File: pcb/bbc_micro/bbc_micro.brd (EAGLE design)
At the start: 56 x 65 mm, 51 parts, among them IC1 STM32F072C8T6, SW1 324_SW, SW2 324_SW, SW3 324_SW

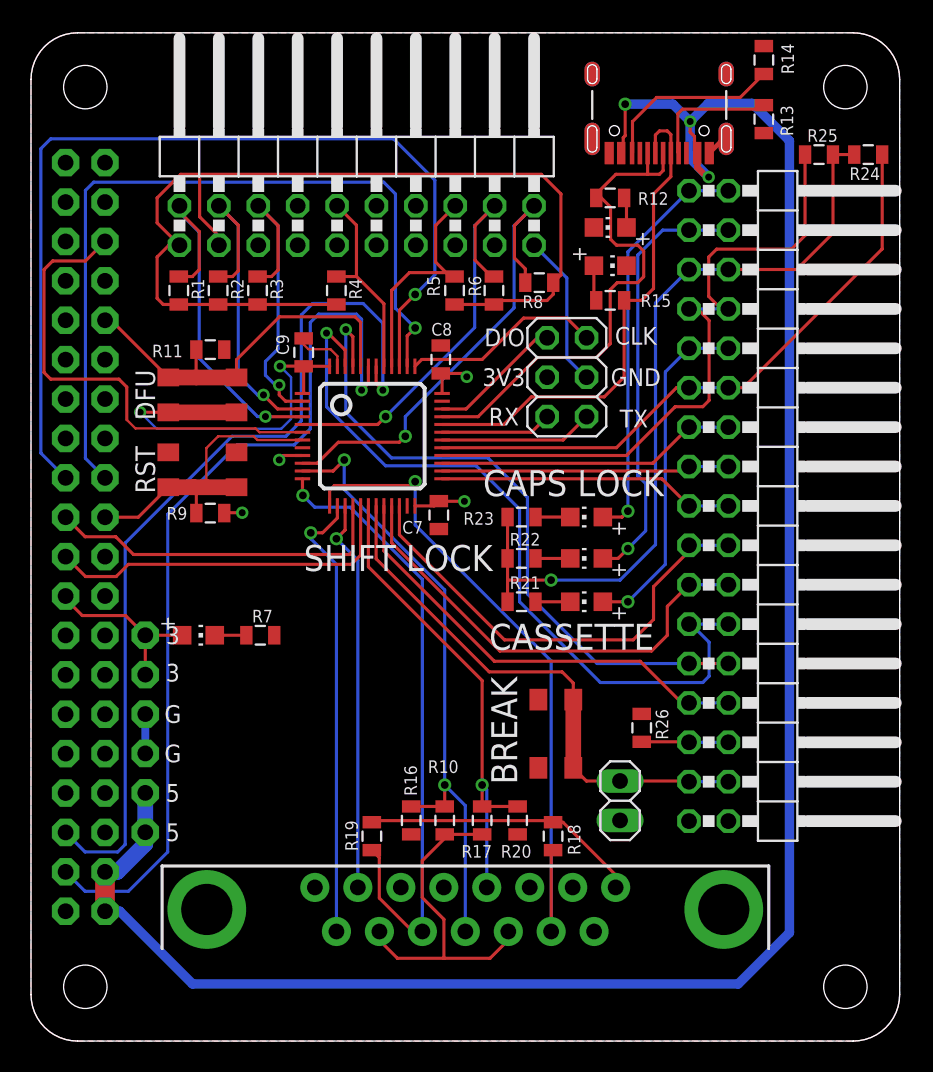
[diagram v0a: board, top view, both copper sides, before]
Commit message: removed second joystick and added BBC VREF input
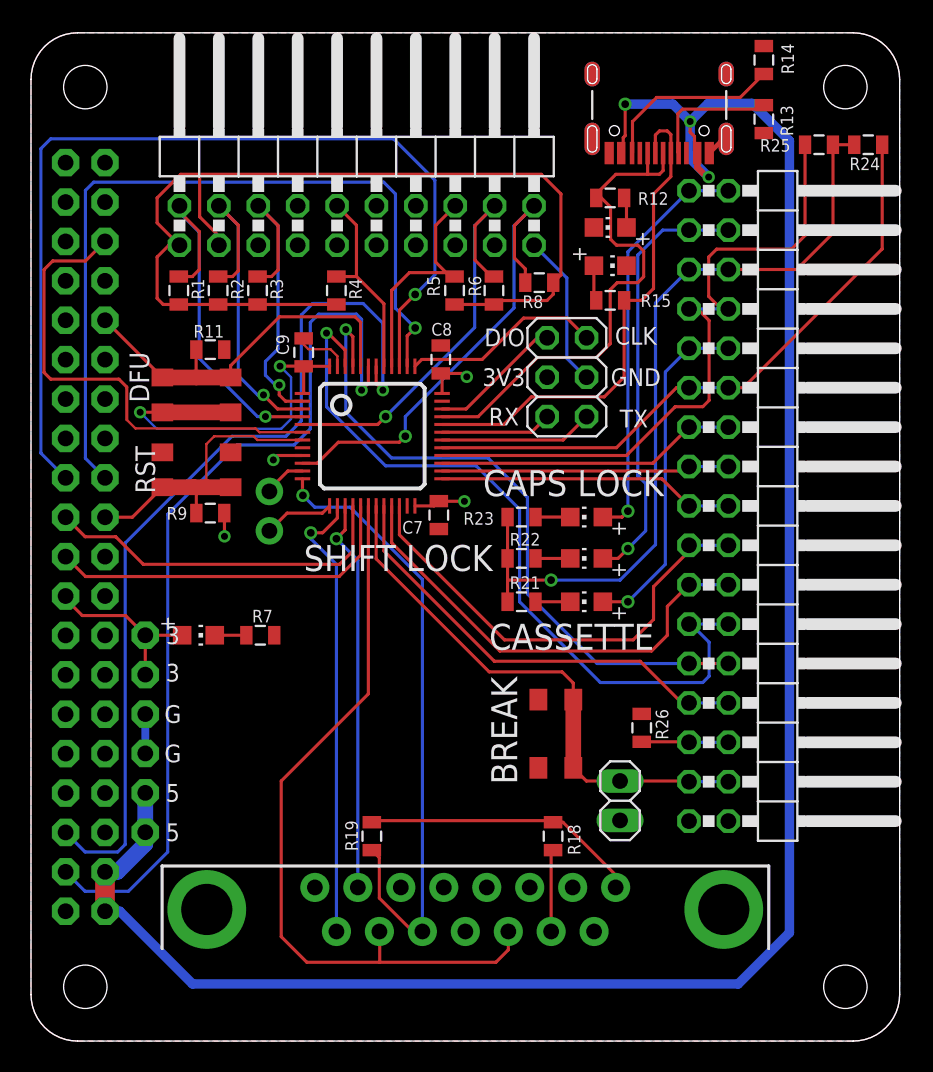
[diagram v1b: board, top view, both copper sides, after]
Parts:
- removed R10, R16, R17, R20: 5.1K, SparkFun-Passives:0805
- added JP10, JP11: (no value), adafruit_changed:1X01-CLEANBIG
- moved R24 0.63 mm to (54.0, 57.8)
- moved R25 0.63 mm to (50.8, 57.8)
- moved SW1 0.38 mm to (10.7, 36.8)
- moved SW2 0.38 mm to (10.7, 41.7)
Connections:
- removed net N$17: IC1.11, R10.2, R16.1, U$9.12
- new net N$11: IC1.11, JP10.1
- net GND: no longer R16.2, R20.2
- net N$10: now also IC1.18; no longer R10.1, R17.1
- net N$12: now also IC1.13, JP11.1; no longer IC1.18, R17.2, R20.1, U$9.4
- net N$21: no longer IC1.13
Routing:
- net N$17: track 40.2 -> 0.00 mm, vias 2 -> 0
- net N$21: track 44.7 -> 5.30 mm, vias 1 -> 0
- net N$10: track 22.0 -> 48.9 mm
- net N$12: track 31.4 -> 4.55 mm, vias 1 -> 0
- net N$11: track 0.00 -> 2.75 mm
- net CA2: track 44.1 -> 44.8 mm
- net W: track 39.8 -> 40.4 mm
- net KB_5V: track 51.3 -> 51.9 mm
- net SPI_MISO: track 22.5 -> 23.0 mm

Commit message: added a pot, clean up
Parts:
- added R10: (no value), SparkFun-Retired:TRIM_POT_PTH
- moved R24 0.13 mm to (54.0, 57.9)
- moved R25 0.13 mm to (50.8, 57.9)
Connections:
- net +3V3: now also R10.3
- net GND: now also R10.1
- net N$12: now also R10.2
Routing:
- net N$12: track 4.55 -> 14.2 mm
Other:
- board text added: "ACT"
- board text added: "ERR"
- board text added: "PIN1"
- board text added: "PT4 dekuNukem OCT2022"
- board text added: "PWR"
- board text removed: "PT3 dekuNukem SEPT2022"
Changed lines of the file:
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@@
 <text x="38.989" y="42.799" size="1.143" layer="25" rot="R180" align="center">GND</text>
 <text x="34.9758" y="35.9664" size="1.6764" layer="25" align="center">CAPS LOCK</text>
-<text x="7.366" y="36.83" size="1.27" layer="25" rot="R90" align="center">RST</text>
+<text x="6.858" y="36.83" size="1.27" layer="25" rot="R90" align="center">RST</text>
 <text x="30.48" y="40.259" size="1.143" layer="25" rot="R180" align="center">RX</text>
 <text x="38.862" y="40.132" size="1.143" layer="25" rot="R180" align="center">TX</text>
-<text x="6.985" y="42.799" size="1.27" layer="25" rot="R90" align="center">DFU</text>
+<text x="6.858" y="42.799" size="1.27" layer="25" rot="R90" align="center">DFU</text>
 <text x="24.3078" y="24.2316" size="1.778" layer="26" rot="MR180" align="center">USB4VC Protocol Card for
 BBC Micro
 </text>
-<text x="24.4348" y="21.1836" size="1.6764" layer="26" rot="MR180" align="center">PT3 dekuNukem SEPT2022</text>
+<text x="24.4348" y="21.1836" size="1.6764" layer="26" rot="MR180" align="center">PT4 dekuNukem OCT2022</text>
 <text x="24.8158" y="17.5006" size="1.9304" layer="26" rot="MR180" align="center">usb4vc.com</text>
 <text x="9.144" y="13.462" size="1.143" layer="25" rot="R180" align="center">5</text>
@@
 <text x="23.6728" y="31.1404" size="1.6764" layer="25" align="center">SHIFT LOCK</text>
 <text x="30.5054" y="20.0152" size="1.6764" layer="25" rot="R270" align="center">BREAK</text>
+<text x="40.386" y="53.34" size="1.4224" layer="25" rot="R270" align="center">ERR</text>
+<text x="40.386" y="48.768" size="1.4224" layer="25" rot="R270" align="center">ACT</text>
+<text x="10.795" y="28.194" size="1.27" layer="25" rot="R180" align="center">PWR</text>
+<text x="7.747" y="61.595" size="1.778" layer="25" ratio="10" rot="R270" align="center">PIN1</text>
 </plain>
 <attributes>
@@
 </element>
 <element name="R12" library="SparkFun-Passives" package="0805" value="2K" x="37.338" y="54.356" smashed="yes">
-<attribute name="NAME" x="41.0972" y="54.7243" size="0.8128" layer="25" rot="R180"/>
+<attribute name="NAME" x="34.8107" y="55.5752" size="0.8128" layer="25" rot="R270"/>
 </element>
 <element name="IC1" library="clock" package="TQFP48" value="STM32F072C8T6" x="22" y="39" smashed="yes" rot="R270"/>
@@
 </element>
 <element name="R15" library="SparkFun-Passives" package="0805" value="2K" x="37.338" y="47.752" smashed="yes" rot="R180">
-<attribute name="NAME" x="39.2938" y="47.3329" size="0.8128" layer="25"/>
+<attribute name="NAME" x="35.7251" y="47.0408" size="0.8128" layer="25" rot="R90"/>
 </element>
 <element name="SW3" library="3pos_slide_switch_centered" package="342_SWICH_FOOT" value="324_SW" x="33.8328" y="19.812" smashed="yes" rot="R270"/>
@@
 <attribute name="NAME" x="29.845" y="34.0995" size="0.8128" layer="25" rot="R180"/>
 </element>
-<element name="R24" library="SparkFun-Passives" package="0805" value="2K" x="53.975" y="57.785" smashed="yes" rot="R180">
-<attribute name="NAME" x="54.737" y="56.9595" size="0.8128" layer="25" rot="R180"/>
-</element>
-<element name="R25" library="SparkFun-Passives" package="0805" value="2K" x="50.8" y="57.785" smashed="yes">
-<attribute name="NAME" x="46.99" y="57.3405" size="0.8128" layer="25"/>
+<element name="R24" library="SparkFun-Passives" package="0805" value="2K" x="53.975" y="57.912" smashed="yes" rot="R180">
+<attribute name="NAME" x="54.737" y="57.0865" size="0.8128" layer="25" rot="R180"/>
+</element>
+<element name="R25" library="SparkFun-Passives" package="0805" value="2K" x="50.8" y="57.912" smashed="yes">
+<attribute name="NAME" x="47.244" y="57.0865" size="0.8128" layer="25"/>
 </element>
 <element name="R26" library="SparkFun-Passives" package="0805" value="5.1K" x="39.37" y="20.193" smashed="yes" rot="R90">
@@
 <element name="JP11" library="adafruit_changed" package="1X01-CLEANBIG" value="" x="15.367" y="32.893" smashed="yes">
 <attribute name="VALUE" x="14.097" y="29.718" size="1.27" layer="27"/>
+</element>
+<element name="R10" library="SparkFun-Retired" package="TRIM_POT_PTH" value="" x="14.478" y="21.082" smashed="yes">
+<attribute name="NAME" x="13.843" y="17.526" size="0.6096" layer="25"/>
+<attribute name="PROD_ID" value="RES-08445" x="14.478" y="21.082" size="1.778" layer="27" display="off"/>
+<attribute name="VALUE" x="17.653" y="21.082" size="0.6096" layer="27"/>
 </element>
 </elements>
@@
 <contactref element="R26" pad="2"/>
 <contactref element="JP5" pad="2"/>
+<contactref element="R10" pad="1"/>
 </signal>
 <signal name="+3V3">
@@
 <wire x1="17.5" y1="37.75" x2="15.906" y2="37.75" width="0.2032" layer="1"/>
 <wire x1="15.906" y1="37.75" x2="15.621" y2="37.465" width="0.2032" layer="1"/>
+<contactref element="R10" pad="3"/>
 </signal>
 <signal name="N$29">
@@
 <wire x1="42.418" y1="42.12" x2="44.958" y2="42.12" width="0.2032" layer="16"/>
 <contactref element="R24" pad="1"/>
-<wire x1="54.875" y1="57.785" x2="54.875" y2="51.065" width="0.2032" layer="1"/>
+<wire x1="54.875" y1="57.912" x2="54.875" y2="51.065" width="0.2032" layer="1"/>
 <wire x1="45.93" y1="42.12" x2="44.958" y2="42.12" width="0.2032" layer="1"/>
 <wire x1="54.875" y1="51.065" x2="45.93" y2="42.12" width="0.2032" layer="1"/>
@@
 <wire x1="42.418" y1="47.2" x2="44.958" y2="47.2" width="0.2032" layer="16"/>
 <contactref element="R25" pad="1"/>
-<wire x1="49.9" y1="57.785" x2="49.9" y2="51.932" width="0.2032" layer="1"/>
+<wire x1="49.9" y1="57.912" x2="49.9" y2="51.932" width="0.2032" layer="1"/>
 <wire x1="49.9" y1="51.932" x2="49.022" y2="51.054" width="0.2032" layer="1"/>
 <wire x1="49.022" y1="51.054" x2="44.196" y2="51.054" width="0.2032" layer="1"/>
@@
 <contactref element="R25" pad="2"/>
 <wire x1="44.958" y1="49.74" x2="49.359" y2="49.74" width="0.2032" layer="1"/>
-<wire x1="51.7" y1="52.081" x2="51.7" y2="57.785" width="0.2032" layer="1"/>
+<wire x1="51.7" y1="52.081" x2="51.7" y2="57.912" width="0.2032" layer="1"/>
 <wire x1="49.359" y1="49.74" x2="51.7" y2="52.081" width="0.2032" layer="1"/>
-<wire x1="53.075" y1="57.785" x2="51.7" y2="57.785" width="0.2032" layer="1"/>
+<wire x1="53.075" y1="57.912" x2="51.7" y2="57.912" width="0.2032" layer="1"/>
 </signal>
 <signal name="LED_SHIFTLOCK">
@@
 <contactref element="U$9" pad="11"/>
 <contactref element="IC1" pad="18"/>
-<wire x1="21.75" y1="34.5" x2="21.75" y2="22.385" width="0.2032" layer="1"/>
-<wire x1="21.75" y1="22.385" x2="16.129" y2="16.764" width="0.2032" layer="1"/>
-<wire x1="16.129" y1="16.764" x2="16.129" y2="6.731" width="0.2032" layer="1"/>
+<wire x1="21.75" y1="34.5" x2="21.75" y2="19.591" width="0.2032" layer="1"/>
+<wire x1="21.75" y1="19.591" x2="16.129" y2="13.97" width="0.2032" layer="1"/>
+<wire x1="16.129" y1="13.97" x2="16.129" y2="6.731" width="0.2032" layer="1"/>
 <wire x1="16.129" y1="6.731" x2="17.78" y2="5.08" width="0.2032" layer="1"/>
 <wire x1="17.78" y1="5.08" x2="22.479" y2="5.08" width="0.2032" layer="1"/>
@@
 <contactref element="IC1" pad="13"/>
 <contactref element="JP11" pad="1"/>
-<wire x1="19.25" y1="34.5" x2="18.786" y2="34.036" width="0.2032" layer="1"/>
-<wire x1="16.51" y1="34.036" x2="15.367" y2="32.893" width="0.2032" layer="1"/>
-<wire x1="18.786" y1="34.036" x2="16.51" y2="34.036" width="0.2032" layer="1"/>
+<wire x1="19.25" y1="34.5" x2="18.659" y2="33.909" width="0.2032" layer="1"/>
+<wire x1="16.383" y1="33.909" x2="15.367" y2="32.893" width="0.2032" layer="1"/>
+<wire x1="18.659" y1="33.909" x2="16.383" y2="33.909" width="0.2032" layer="1"/>
+<contactref element="R10" pad="2"/>
+<wire x1="15.367" y1="32.893" x2="15.367" y2="24.511" width="0.2032" layer="16"/>
+<wire x1="15.367" y1="24.511" x2="14.478" y2="23.622" width="0.2032" layer="16"/>
 </signal>
 </signals>
